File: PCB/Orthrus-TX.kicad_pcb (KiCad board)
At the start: 8 copper layers, 49 x 49 mm, 136 parts, among them J1 HRO-TYPE-C-31-M-13x, U2 SRV05-4, U3 SRV05-4, U4 SRV05-4

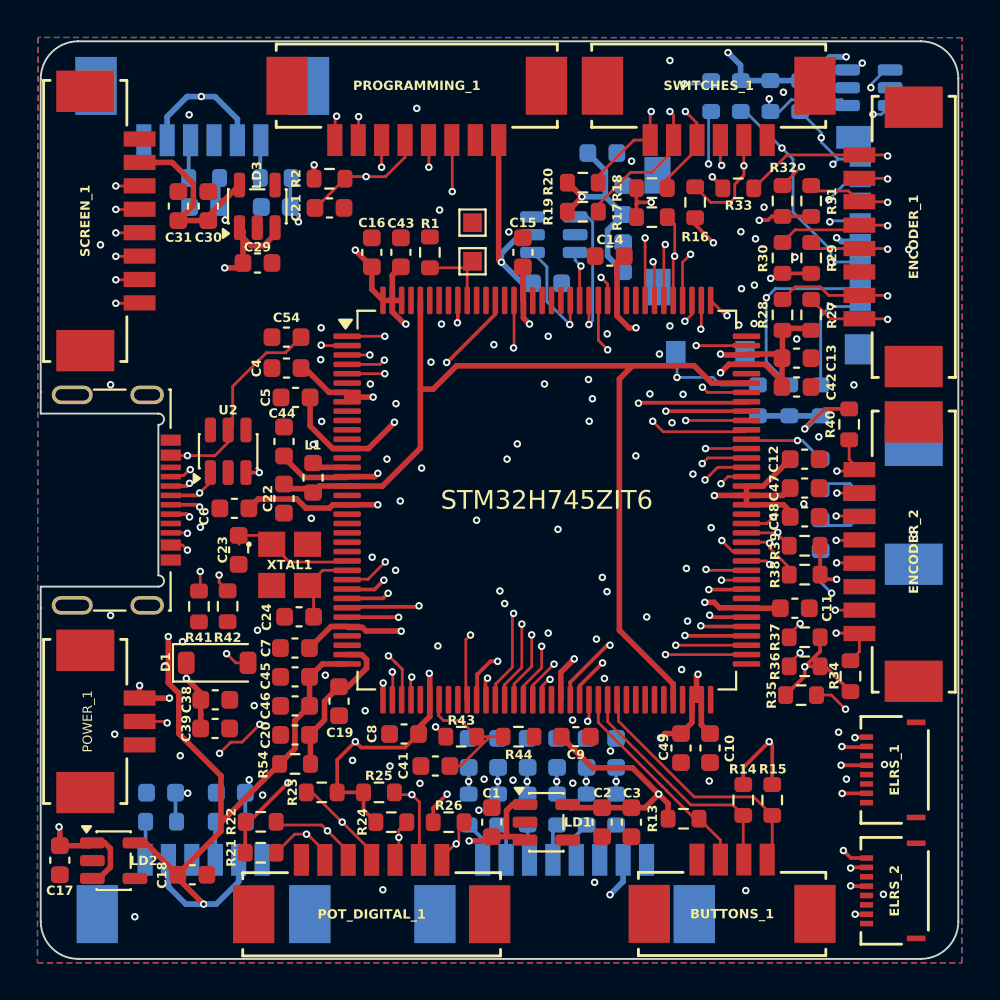
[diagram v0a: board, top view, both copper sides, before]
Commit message: extra GND vias
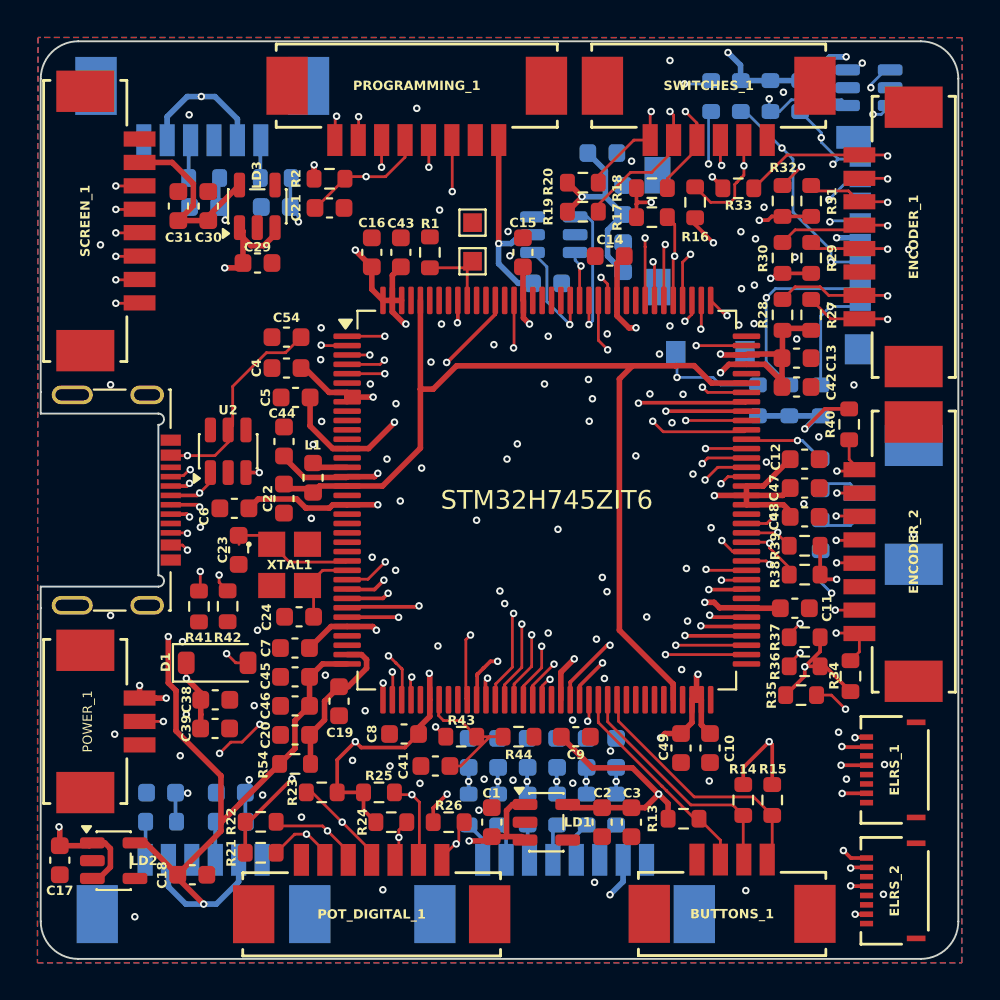
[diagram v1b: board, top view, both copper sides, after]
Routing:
- net /LD1_3.3v: track 250.4 -> 248.6 mm
- net GND: vias 81 -> 85

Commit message: adjust the USB traces
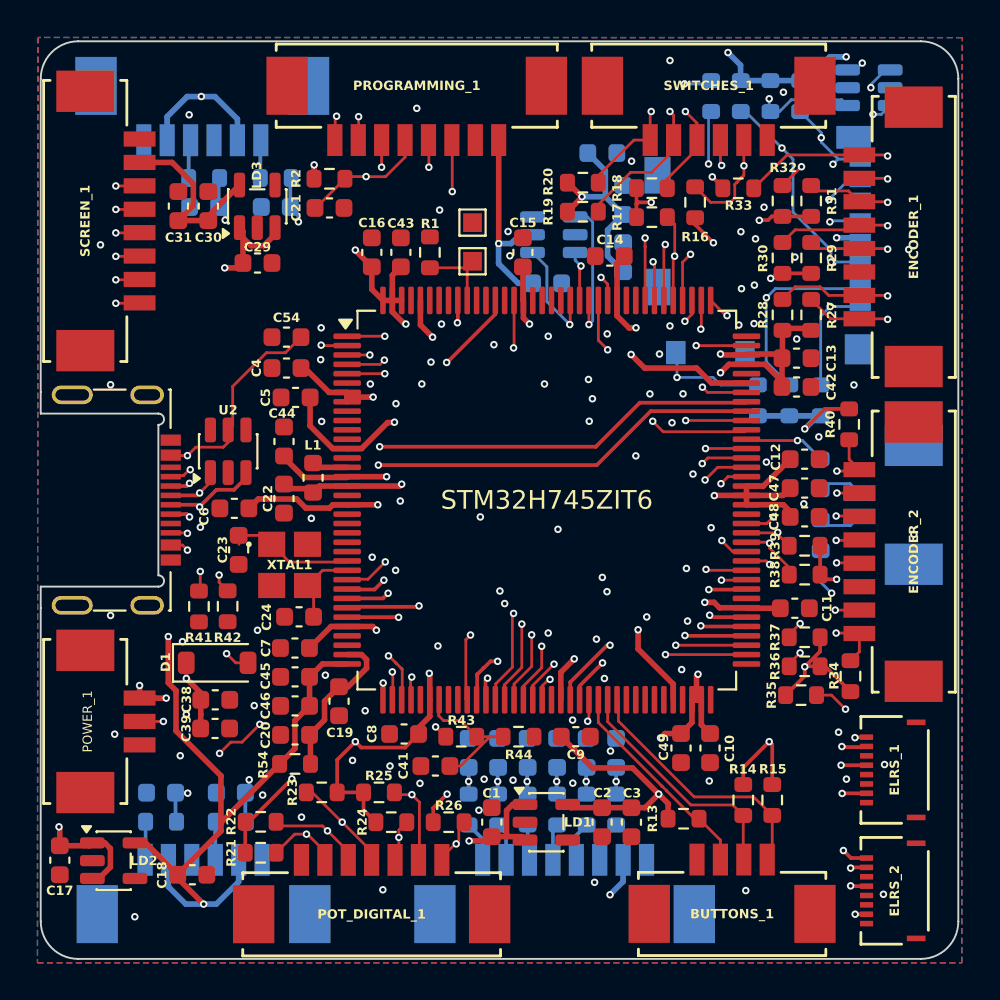
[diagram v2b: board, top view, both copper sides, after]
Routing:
- net /USB_N: track 36.4 -> 39.1 mm, vias 6 -> 3
- net /VCAP: track 54.0 -> 55.0 mm, vias 0 -> 4
- net /USB_P: track 36.8 -> 37.2 mm, vias 5 -> 3

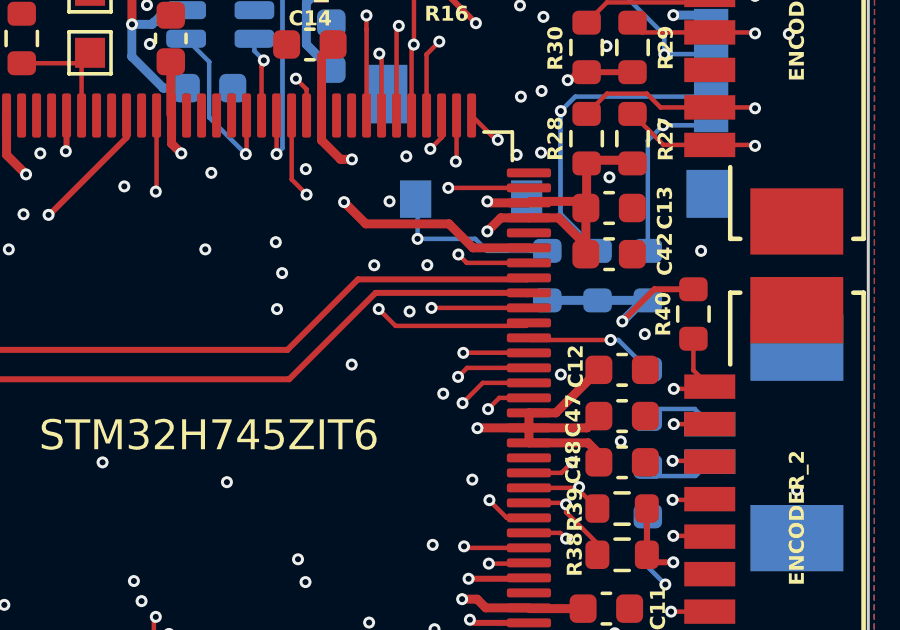
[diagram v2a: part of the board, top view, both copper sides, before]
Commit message: small adjustment for the logo
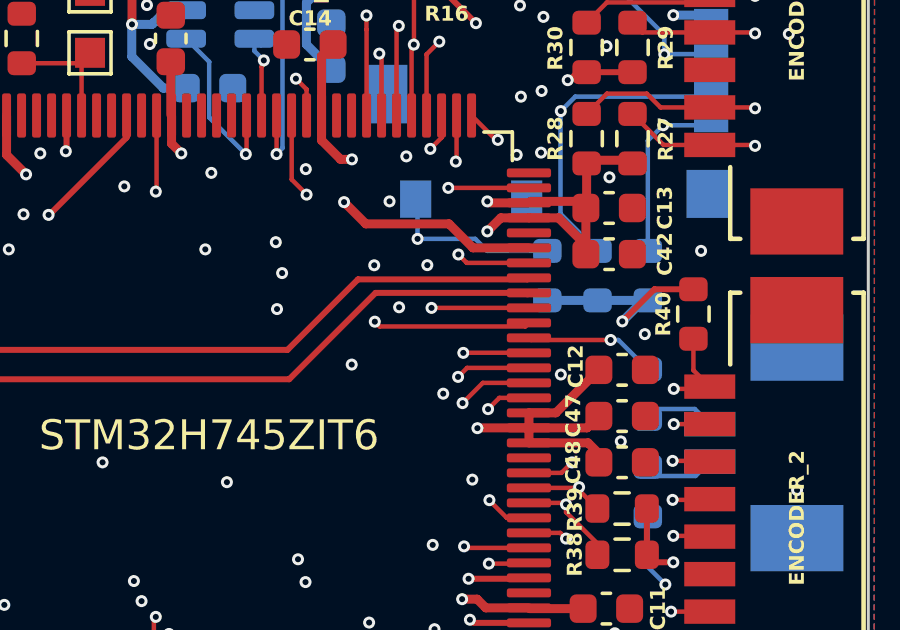
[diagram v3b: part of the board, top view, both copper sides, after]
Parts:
- moved Orthrus TX 0.36 mm to (147.8, 59.0)
